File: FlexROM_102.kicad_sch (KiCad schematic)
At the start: 6 parts

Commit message: FlexROM_102 outline, sch
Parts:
- J1: value (none) -> 27C256 DIP LEGS; footprint (none) -> 000_LOCAL:DIP28_0.6_pcb
- JP1: value (none) -> ~{CS} breakout (REX TP1); footprint (none) -> 000_LOCAL:Pin_Header_Angled_1x02_Pitch2.54mm
- JP2: value (none) -> Jumper_4_Bridged23; footprint (none) -> 000_LOCAL:PinHeader_1x04_P2.00mm_Horizontal
- R1, R2: value (none) -> 47K; footprint (none) -> 000_LOCAL:R_0805
- U1: value (none) -> 28C256; footprint (none) -> 000_LOCAL:SOIC28W
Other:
- note added: "RUN / PROGRAM"
- note added: "RUN mode (27C256 pinout on DIP legs): 1 2 3 4 PROGRAM mode (28C256 pinout on DIP legs): 1 2 3 4"
- note removed: "PROGRAM mode (28C256 pinout on DIP legs): 1 2 3 4"
- note removed: "RUN mode (27C256 pinout on DIP legs): 1 2 3 4"
- moved on the sheet: JP1, JP2, R1, R2

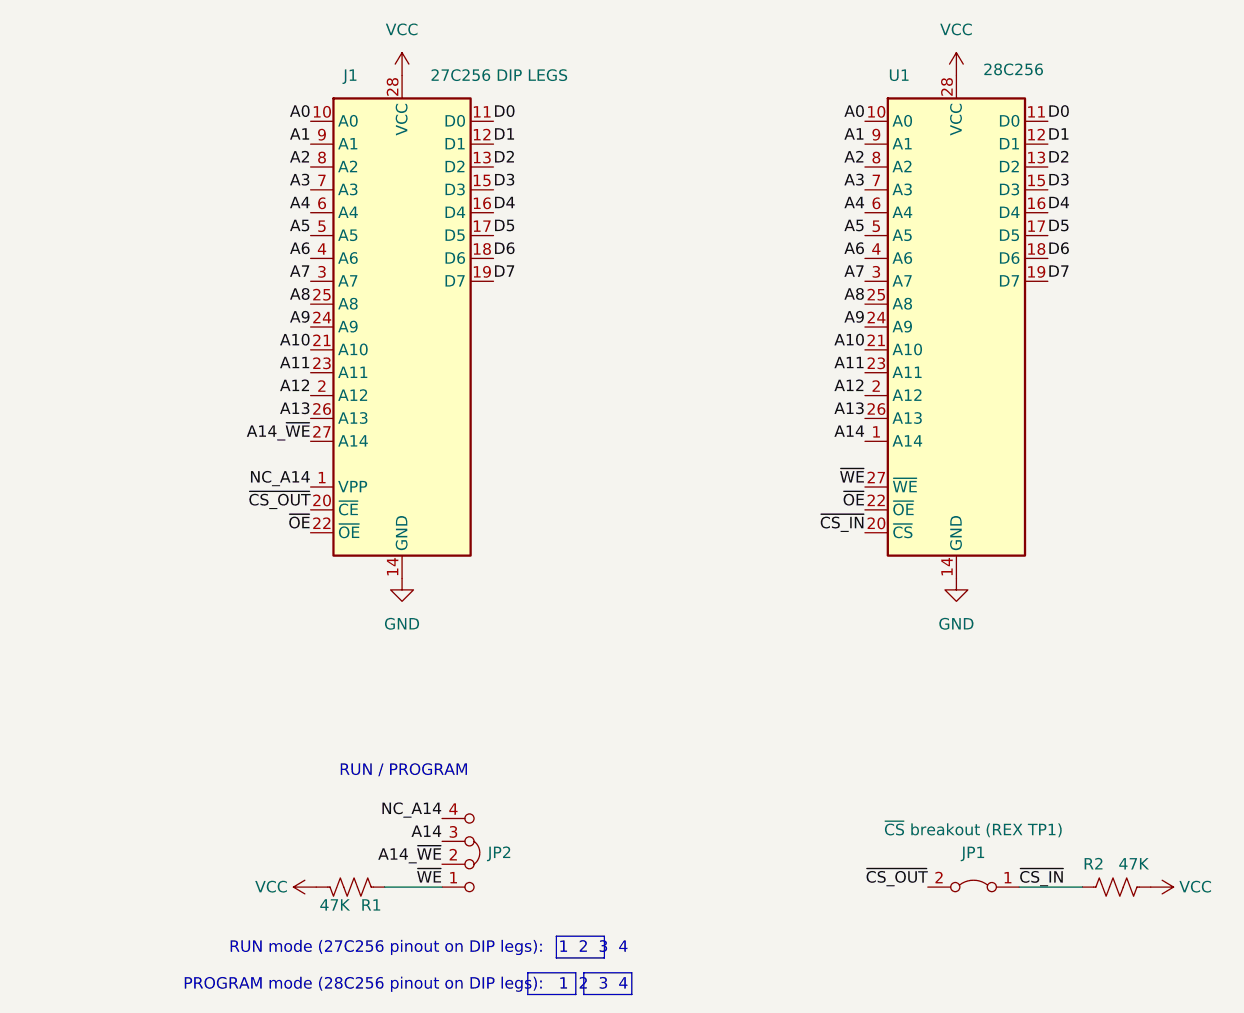
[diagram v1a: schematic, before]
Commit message: flexrom 102 & 200 accept eeprom or fram
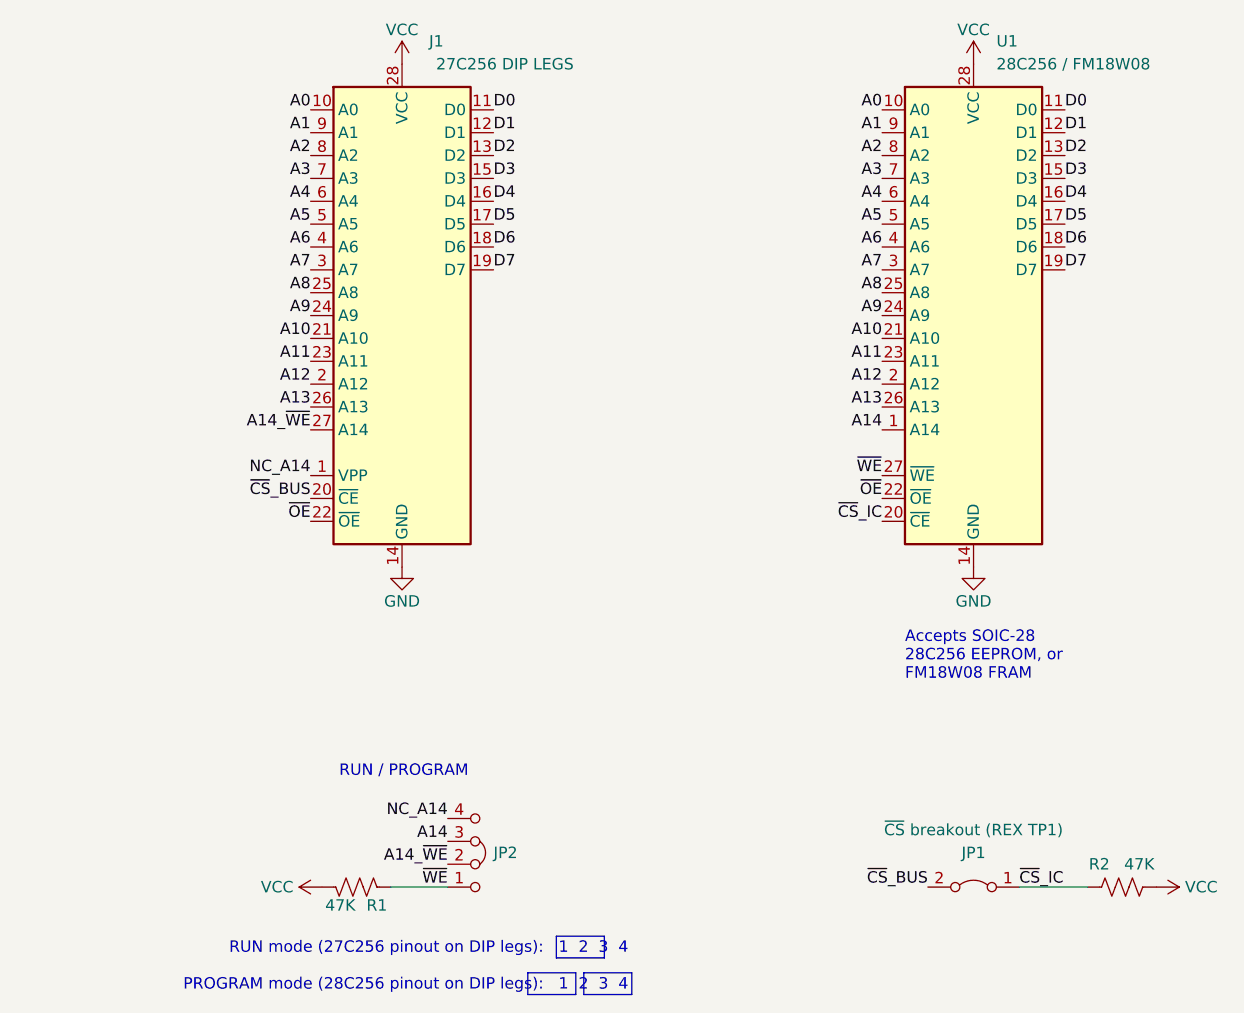
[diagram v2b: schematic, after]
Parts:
- U1: value 28C256 -> 28C256 / FM18W08; footprint 000_LOCAL:SOIC28W -> (none)
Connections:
- net ~{CS_IN} renamed ~{CS}_IC
- net ~{CS_OUT} renamed ~{CS}_BUS
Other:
- note added: "Accepts SOIC-28 28C256 EEPROM, or FM18W08 FRAM"
- moved on the sheet: J1, JP2, R1, R2

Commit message: minor touches
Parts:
- added C1: 0.1uF, 000_LOCAL:C_0805, symbol 000_LOCAL:C_Small
- R1, R2: value 47K -> 100K
- U1: footprint (none) -> 000_LOCAL:SOIC28W
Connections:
- net GND: now also C1.2
- net VCC: now also C1.1
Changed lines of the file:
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@@
   (title_block
     (title "28C256 SOIC to 27C256 DIP")
-    (date "2022-11-30")
-    (rev "004")
+    (date "2023-01-12")
+    (rev "005")
     (company "Brian K. White - b.kenyon.w@gmail.com")
-    (comment 1 "TRS-80 Model 102 system rom M12")
-    (comment 2 "Support REX main rom feature")
   )
   (polyline (pts (xy 128.143 149.225) (xy 128.143 151.638))
@@
   (symbol (lib_id "000_LOCAL:R_US") (at 187.96 139.7 90) (unit 1)
     (in_bom yes) (on_board yes)
-    (property "Reference" "R2" (id 0) (at 185.42 137.16 90))
-    (property "Value" "47K" (id 1) (at 189.865 137.16 90))
+    (property "Reference" "R2" (id 0) (at 187.96 137.16 90))
+    (property "Value" "100K" (id 1) (at 187.96 142.24 90))
     (property "Footprint" "000_LOCAL:R_0805" (id 2) (at 187.96 139.7 0)
       (effects (font (size 1.27 1.27)) hide)
@@
   (symbol (lib_id "000_LOCAL:R_US") (at 102.87 139.7 90) (mirror x) (unit 1)
     (in_bom yes) (on_board yes)
-    (property "Reference" "R1" (id 0) (at 105.156 141.732 90))
-    (property "Value" "47K" (id 1) (at 101.092 141.732 90))
+    (property "Reference" "R1" (id 0) (at 102.87 137.16 90))
+    (property "Value" "100K" (id 1) (at 102.87 142.24 90))
     (property "Footprint" "000_LOCAL:R_0805" (id 2) (at 102.87 139.7 0)
       (effects (font (size 1.27 1.27)) hide)
@@
     (pin "4")
   )
+  (symbol (lib_id "000_LOCAL:C_Small") (at 146.05 50.8 0) (unit 1)
+    (in_bom yes) (on_board yes) (fields_autoplaced)
+    (property "Reference" "C1" (id 0) (at 148.59 49.5362 0)
+      (effects (font (size 1.27 1.27)) (justify left))
+    )
+    (property "Value" "0.1uF" (id 1) (at 148.59 52.0762 0)
+      (effects (font (size 1.27 1.27)) (justify left))
+    )
+    (property "Footprint" "000_LOCAL:C_0805" (id 2) (at 146.05 50.8 0)
+      (effects (font (size 1.27 1.27)) hide)
+    )
+    (property "Datasheet" "~" (id 3) (at 146.05 50.8 0)
+      (effects (font (size 1.27 1.27)) hide)
+    )
+    (pin "1")
+    (pin "2")
+  )
   (symbol (lib_id "000_LOCAL:VCC") (at 171.45 48.26 0) (unit 1)
     (in_bom yes) (on_board yes)
@@
     (pin "1")
   )
+  (symbol (lib_id "000_LOCAL:VCC") (at 146.05 48.26 0) (unit 1)
+    (in_bom yes) (on_board yes)
+    (property "Reference" "#PWR0108" (id 0) (at 146.05 52.07 0)
+      (effects (font (size 1.27 1.27)) hide)
+    )
+    (property "Value" "VCC" (id 1) (at 146.05 44.45 0))
+    (property "Footprint" "" (id 2) (at 146.05 48.26 0)
+      (effects (font (size 1.27 1.27)) hide)
+    )
+    (property "Datasheet" "" (id 3) (at 146.05 48.26 0)
+      (effects (font (size 1.27 1.27)) hide)
+    )
+    (pin "1")
+  )
   (symbol (lib_id "000_LOCAL:VCC") (at 191.77 139.7 270) (unit 1)
     (in_bom yes) (on_board yes)
@@
       (effects (font (size 1.27 1.27)) (justify left))
     )
-    (property "Footprint" "" (id 2) (at 171.45 76.2 0)
+    (property "Footprint" "000_LOCAL:SOIC28W" (id 2) (at 171.45 76.2 0)
       (effects (font (size 1.27 1.27)) hide)
     )
@@
     (pin "1")
   )
+  (symbol (lib_id "000_LOCAL:GND") (at 146.05 53.34 0) (unit 1)
+    (in_bom yes) (on_board yes)
+    (property "Reference" "#PWR0107" (id 0) (at 146.05 59.69 0)
+      (effects (font (size 1.27 1.27)) hide)
+    )
+    (property "Value" "GND" (id 1) (at 146.05 57.15 0))
+    (property "Footprint" "" (id 2) (at 146.05 53.34 0)
+      (effects (font (size 1.27 1.27)) hide)
+    )
+    (property "Datasheet" "" (id 3) (at 146.05 53.34 0)
+      (effects (font (size 1.27 1.27)) hide)
+    )
+    (pin "1")
+  )
   (sheet_instances
     (path "/" (page "1"))
@@
       (reference "#PWR0106") (unit 1) (value "VCC") (footprint "")
     )
+    (path "/f29824ea-10b9-489b-bf5d-4bf9342cd2eb"
+      (reference "#PWR0107") (unit 1) (value "GND") (footprint "")
+    )
+    (path "/ac7a2258-c5e0-45b9-a22d-ee2658914a92"
+      (reference "#PWR0108") (unit 1) (value "VCC") (footprint "")
+    )
+    (path "/158b3a4e-f997-4762-ba41-2c628a9da99b"
+      (reference "C1") (unit 1) (value "0.1uF") (footprint "000_LOCAL:C_0805")
+    )
     (path "/00000000-0000-0000-0000-00005e5c209e"
       (reference "J1") (unit 1) (value "27C256 DIP LEGS") (footprint "000_LOCAL:DIP28_0.6_pcb")
@@
     )
     (path "/00000000-0000-0000-0000-00005e6b3af8"
-      (reference "R1") (unit 1) (value "47K") (footprint "000_LOCAL:R_0805")
+      (reference "R1") (unit 1) (value "100K") (footprint "000_LOCAL:R_0805")
     )
     (path "/00000000-0000-0000-0000-00005e68c7f8"
-      (reference "R2") (unit 1) (value "47K") (footprint "000_LOCAL:R_0805")
+      (reference "R2") (unit 1) (value "100K") (footprint "000_LOCAL:R_0805")
     )
     (path "/ae14f39a-abe8-4843-8454-0883709a3f97"
-      (reference "U1") (unit 1) (value "28C256 / FM18W08") (footprint "")
-    )
-  )
+      (reference "U1") (unit 1) (value "28C256 / FM18W08") (footprint "000_LOCAL:SOIC28W")
+    )
+  )
